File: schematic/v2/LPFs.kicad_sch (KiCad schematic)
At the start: 30 parts, among them SW4 SW_Nidec_CAS-120A1, SW5 SW_Nidec_CAS-120A1, U32 OPA196xDGK, U33 OPA196xDGK, U35 OPA196xDGK, U41 OPA196xDGK, U42 OPA196xDGK

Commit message: some progress on affm board
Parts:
- removed R68: 100k, Resistor_SMD:R_0805_2012Metric_Pad1.20x1.40mm_HandSolder, symbol Device:R
- added SW1: LPF_FBCK_OUT, Button_Switch_SMD:Nidec_Copal_CAS-120A, symbol Switch:SW_Nidec_CAS-120A1
- added SW2: LPF_IN_SW, Button_Switch_SMD:Nidec_Copal_CAS-120A, symbol Switch:SW_Nidec_CAS-120A1
- added VOL_BALANCE: 100k, Potentiometer_THT:Potentiometer_Alps_RK09Y11_Single_Horizontal, symbol Device:R_Potentiometer
- SW4: value SW_Nidec_CAS-120A1 -> LPF_OUT_SW
- SW5: value SW_Nidec_CAS-120A1 -> LPF_FBCK_IN
- renumbered RV1 to PASS_LPF_CUTOFF
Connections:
- net CFBACK_IN: now also SW1.1 (C); no longer C18.2, R70.1, SW5.1 (C), U35.3 (+), U35.6
- net GND: no longer U32.4 (V-), U41.4 (V-), U42.4 (V-)
- net MONO_IN: now also SW2.2 (B); no longer C11.2, PASS_LPF_CUTOFF.1
- net at C11.1, R67.2: now also VOL_BALANCE.1
- net 12V+: now reaches U41.7 (V+)
- net 12V+: now also U32.7 (V+), U33.7 (V+), U35.7 (V+), U42.7 (V+)
- net 12V-: now reaches U33.4 (V-)
- net 12V-: now also U32.4 (V-), U35.4 (V-), U41.4 (V-), U42.4 (V-)
- net at R69.2, U32.3 (+): now also VOL_BALANCE.3
- net LPF_MONO_OUT: now reaches SW4.2 (B)
- new net: C11.2, SW2.1 (C)
- new net: C18.2, SW1.2 (B)
- new net: PASS_LPF_CUTOFF.1, SW2.3 (A)
- new net RFBACK_OUT: R70.1, SW1.3 (A), SW5.1 (C), U35.3 (+), U35.6
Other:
- note added: "This sheet has a couple of LPF implementations choosable via a DIP switch. - Standard "1 pole" passive RC LPF implementation - 4 pole active op amp implementation"
- note added: "Volume balance"
- note removed: "This sheet has a couple of LPF implementations choosable via a DIP switch. - Standard "1 pole" passive RC LPF implementation - Opamp implementaition"
- moved on the sheet: C14, D39, D40, D41, D42, D43, D44, PASS_LPF_CUTOFF, R64, R65, R70, R71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

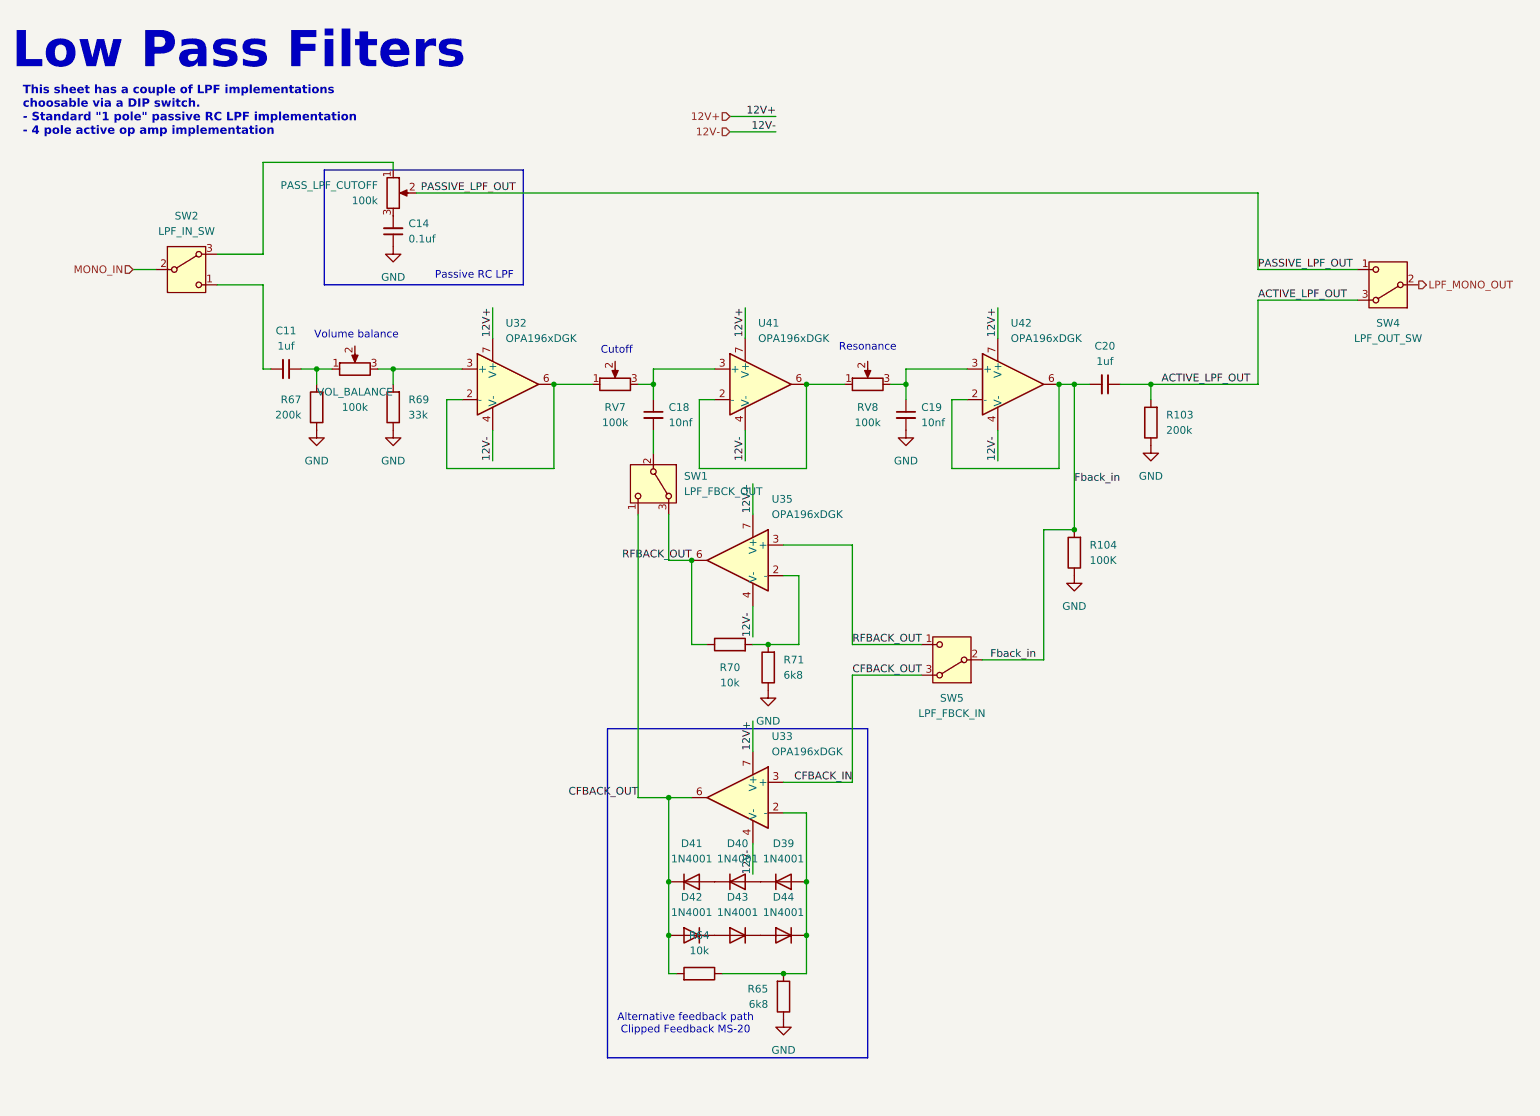
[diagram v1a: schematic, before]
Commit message: now making a v3 with HATs for each nucleo with my needed shit. this will make things very compact and hopefully much cheaper
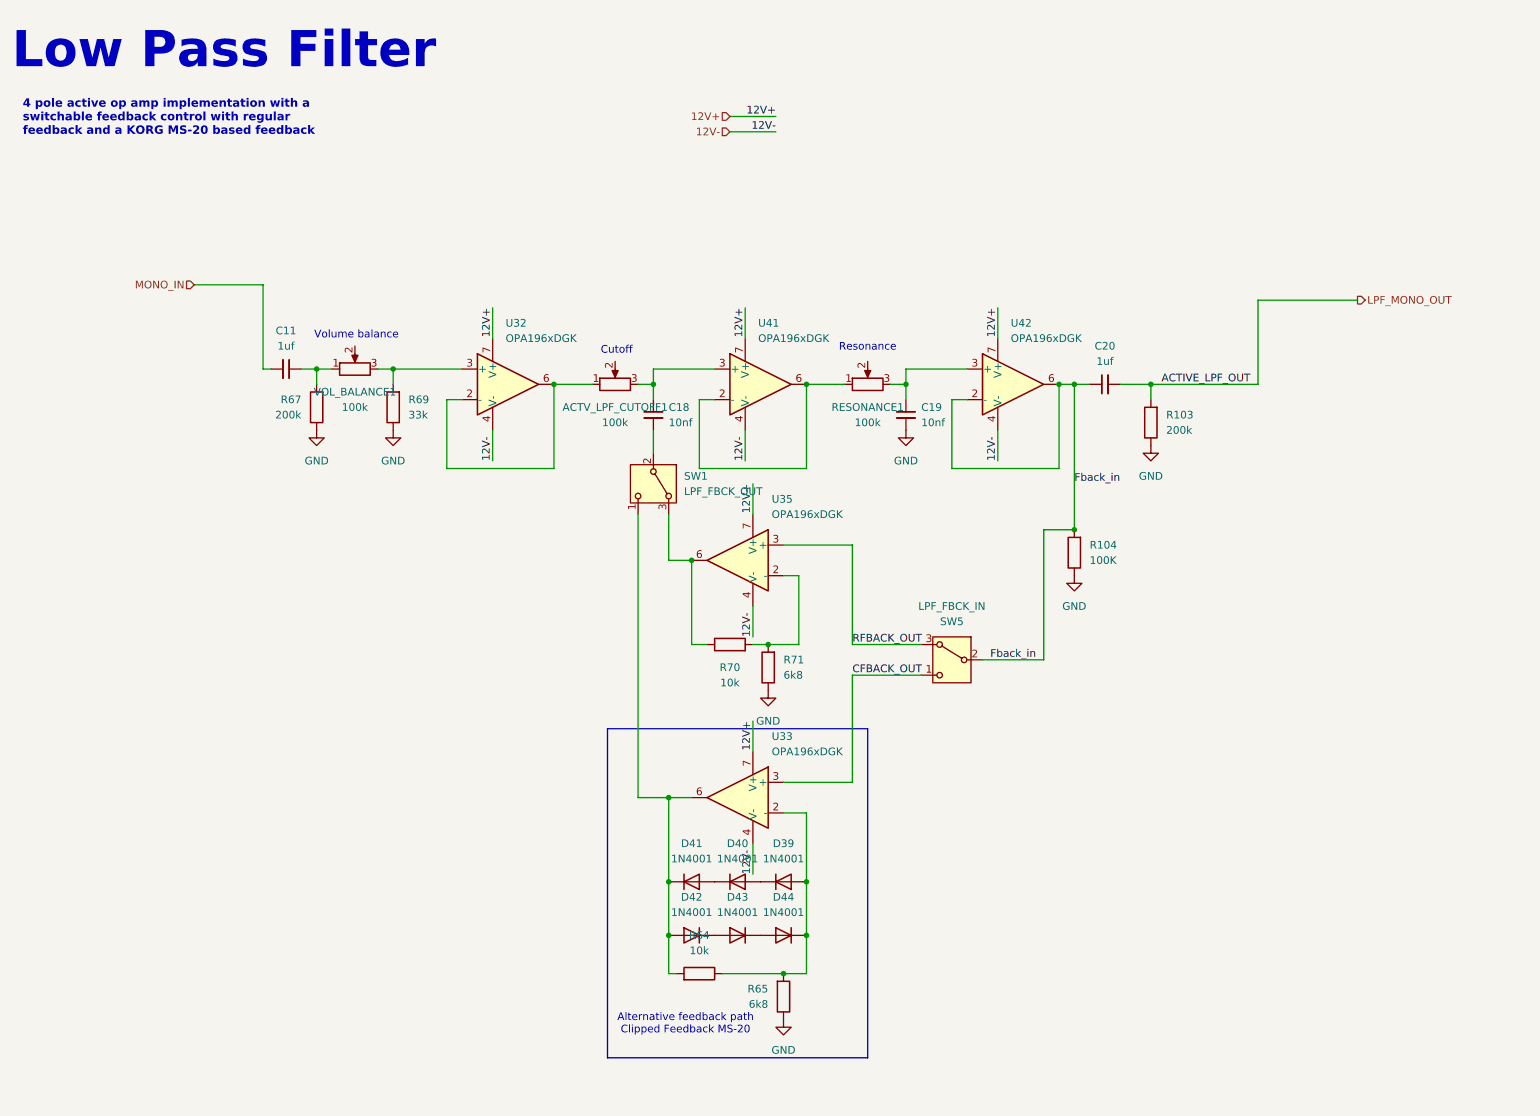
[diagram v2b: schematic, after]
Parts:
- removed C14: 0.1uf, Capacitor_SMD:C_0805_2012Metric, symbol Device:C_Small
- removed PASS_LPF_CUTOFF: 100k, Potentiometer_THT:Potentiometer_Alps_RK09Y11_Single_Horizontal, symbol Device:R_Potentiometer
- removed SW2: LPF_IN_SW, Button_Switch_SMD:Nidec_Copal_CAS-120A, symbol Switch:SW_Nidec_CAS-120A1
- removed SW4: LPF_OUT_SW, Button_Switch_SMD:Nidec_Copal_CAS-120A, symbol Switch:SW_Nidec_CAS-120A1
- renumbered RV7 to ACTV_LPF_CUTOFF1, RV8 to RESONANCE1, VOL_BALANCE to VOL_BALANCE1
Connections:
- net Fback_in: now also C20.1; no longer C20.2
- net LPF_MONO_OUT: now also C20.2, R103.2
- net MONO_IN: now also C11.2
- net RFBACK_OUT: now also SW5.3 (A); no longer R70.1, SW1.3 (A), SW5.1 (C), U35.6
- removed net ACTIVE_LPF_OUT: C20.1, R103.2
- net CFBACK_IN: no longer names the net of D41.1 (K), D42.2 (A), R64.2, SW1.1 (C), U33.6
- net CFBACK_IN: no longer SW5.3 (A), U33.3 (+)
- new net: R70.1, SW1.3 (A), U35.6
- new net CFBACK_OUT: SW5.1 (C), U33.3 (+)
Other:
- note added: "4 pole active op amp implementation with a switchable feedback control with regular feedback and a KORG MS-20 based feedback"
- note added: "Low Pass Filter"
- note removed: "Low Pass Filters"
- note removed: "Passive RC LPF"
- note removed: "This sheet has a couple of LPF implementations choosable via a DIP switch. - Standard "1 pole" passive RC LPF implementation - 4 pole active op amp implementation"
- moved on the sheet: C20, SW5
